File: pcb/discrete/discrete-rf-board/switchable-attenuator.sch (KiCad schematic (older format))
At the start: 11 parts, among them U18 BGS12PL6E6327XTSA1, U19 BGS12PL6E6327XTSA1

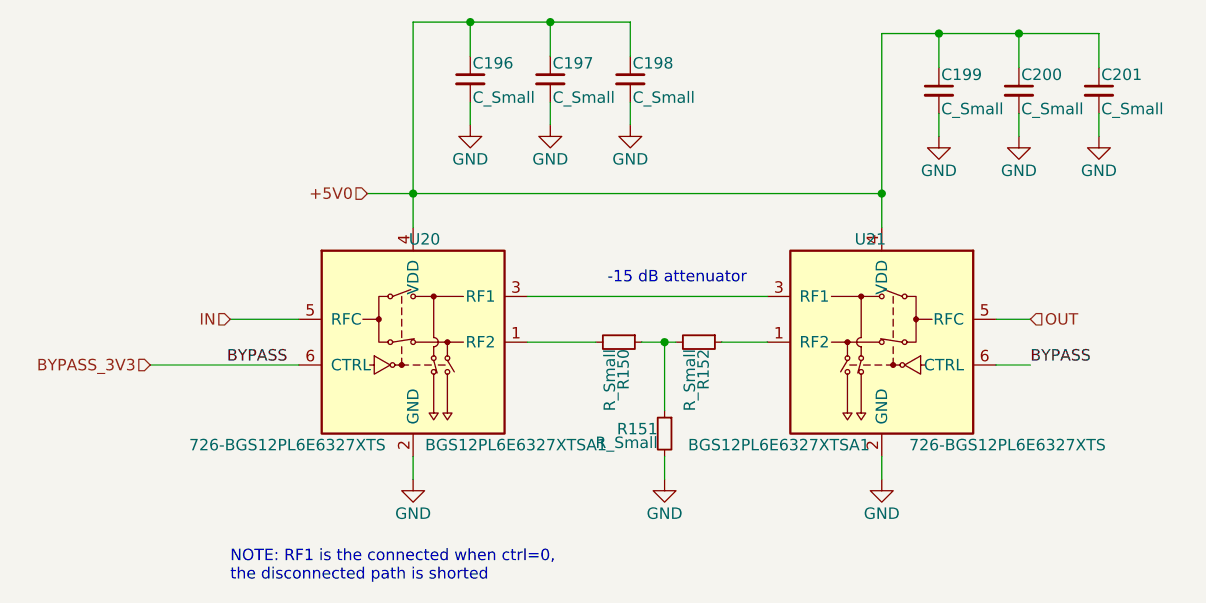
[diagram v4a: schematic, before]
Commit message: All component values set (TODO change transistor gain stages to match values from experimentation
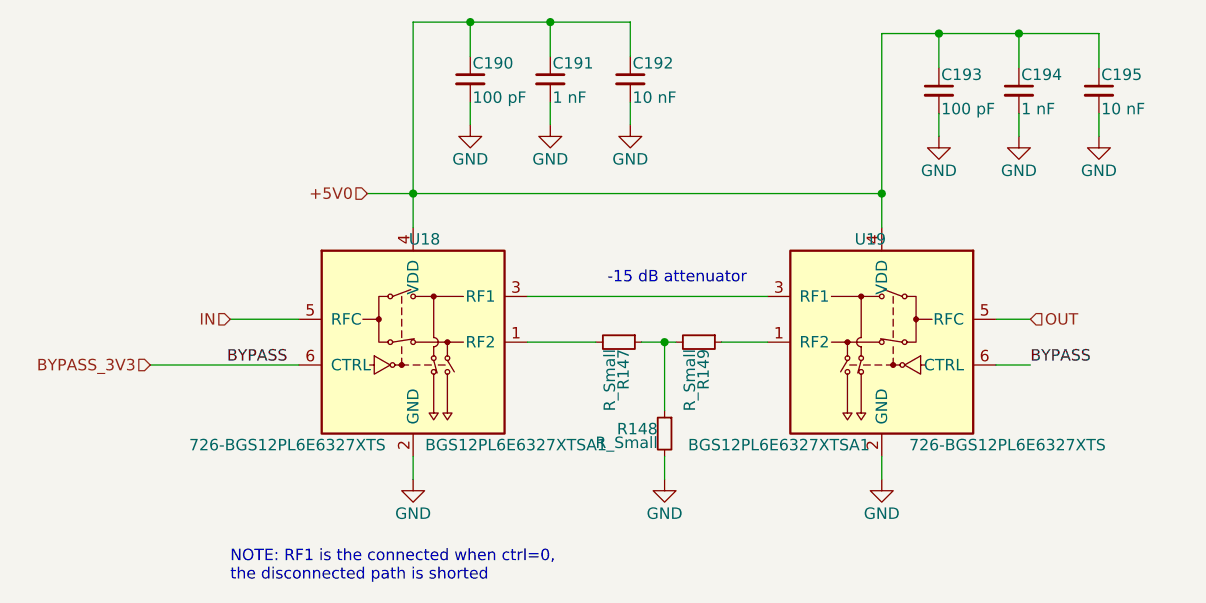
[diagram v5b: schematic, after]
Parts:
- C190, C193: value C_Small -> 100 pF
- C191, C194: value C_Small -> 1 nF
- C192, C195: value C_Small -> 10 nF
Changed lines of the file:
@@
 AR Path="/5CA6B0AA/5CE74EBE/5D4B0AA8/5D4B1FC3" Ref="U18"  Part="1"
 AR Path="/5CA6B0AA/5CE74EBE/5D4C7749/5D4B1FC3" Ref="U20"  Part="1"
-F 0 "U20" H 4000 3750 50  0000 C CNN
+F 0 "U18" H 4000 3750 50  0000 C CNN
 F 1 "BGS12PL6E6327XTSA1" H 4400 2850 50  0000 C CNN
 F 2 "discrete_footprints:Infineon_TSLP-6-4" H 3950 3300 50  0001 C CNN
@@
 AR Path="/5CA6B0AA/5CE74EBE/5D4B0AA8/5D4B1FCA" Ref="R147"  Part="1"
 AR Path="/5CA6B0AA/5CE74EBE/5D4C7749/5D4B1FCA" Ref="R150"  Part="1"
-F 0 "R150" H 4880 3320 50  0000 L CNN
+F 0 "R147" H 4880 3320 50  0000 L CNN
 F 1 "R_Small" H 4880 3260 50  0000 L CNN
 F 2 "" H 4850 3300 50  0001 C CNN
@@
 AR Path="/5CA6B0AA/5CE74EBE/5D4B0AA8/5D4B1FD0" Ref="R149"  Part="1"
 AR Path="/5CA6B0AA/5CE74EBE/5D4C7749/5D4B1FD0" Ref="R152"  Part="1"
-F 0 "R152" H 5230 3320 50  0000 L CNN
+F 0 "R149" H 5230 3320 50  0000 L CNN
 F 1 "R_Small" H 5230 3260 50  0000 L CNN
 F 2 "" H 5200 3300 50  0001 C CNN
@@
 AR Path="/5CA6B0AA/5CE74EBE/5D4B0AA8/5D4B1FD6" Ref="R148"  Part="1"
 AR Path="/5CA6B0AA/5CE74EBE/5D4C7749/5D4B1FD6" Ref="R151"  Part="1"
-F 0 "R151" H 5080 3720 50  0000 L CNN
+F 0 "R148" H 5080 3720 50  0000 L CNN
 F 1 "R_Small" H 5080 3660 50  0000 L CNN
 F 2 "" H 5050 3700 50  0001 C CNN
@@
 AR Path="/5CA6B0AA/5CE74EBE/5D4B0AA8/5D4B1FDD" Ref="#PWR0238"  Part="1"
 AR Path="/5CA6B0AA/5CE74EBE/5D4C7749/5D4B1FDD" Ref="#PWR0247"  Part="1"
-F 0 "#PWR0247" H 3950 3650 50  0001 C CNN
+F 0 "#PWR0238" H 3950 3650 50  0001 C CNN
 F 1 "GND" H 3950 3750 50  0000 C CNN
 F 2 "" H 3950 3900 50  0001 C CNN
@@
 AR Path="/5CA6B0AA/5CE74EBE/5D4B0AA8/5D4B1FE5" Ref="#PWR0242"  Part="1"
 AR Path="/5CA6B0AA/5CE74EBE/5D4C7749/5D4B1FE5" Ref="#PWR0251"  Part="1"
-F 0 "#PWR0251" H 5050 3650 50  0001 C CNN
+F 0 "#PWR0242" H 5050 3650 50  0001 C CNN
 F 1 "GND" H 5050 3750 50  0000 C CNN
 F 2 "" H 5050 3900 50  0001 C CNN
@@
 AR Path="/5CA6B0AA/5CE74EBE/5D4B0AA8/5D4B2001" Ref="#PWR0243"  Part="1"
 AR Path="/5CA6B0AA/5CE74EBE/5D4C7749/5D4B2001" Ref="#PWR0252"  Part="1"
-F 0 "#PWR0252" H 6000 3650 50  0001 C CNN
+F 0 "#PWR0243" H 6000 3650 50  0001 C CNN
 F 1 "GND" H 6000 3750 50  0000 C CNN
 F 2 "" H 6000 3900 50  0001 C CNN
@@
 AR Path="/5CA6B0AA/5CE74EBE/5D4B0AA8/5D4B1FF8" Ref="U19"  Part="1"
 AR Path="/5CA6B0AA/5CE74EBE/5D4C7749/5D4B1FF8" Ref="U21"  Part="1"
-F 0 "U21" H 6050 3750 50  0000 C CNN
+F 0 "U19" H 6050 3750 50  0000 C CNN
 F 1 "BGS12PL6E6327XTSA1" H 6450 2850 50  0000 C CNN
 F 2 "" H 6000 3300 50  0001 C CNN
@@
 AR Path="/5CA6B0AA/5CE74EBE/5D4B0AA8/5D4BC42E" Ref="C190"  Part="1"
 AR Path="/5CA6B0AA/5CE74EBE/5D4C7749/5D4BC42E" Ref="C196"  Part="1"
-F 0 "C196" H 4210 2220 50  0000 L CNN
-F 1 "C_Small" H 4210 2070 50  0000 L CNN
+F 0 "C190" H 4210 2220 50  0000 L CNN
+F 1 "100 pF" H 4210 2070 50  0000 L CNN
 F 2 "" H 4200 2150 50  0001 C CNN
 F 3 "~" H 4200 2150 50  0001 C CNN
@@
 AR Path="/5CA6B0AA/5CE74EBE/5D4B0AA8/5D4BC853" Ref="C191"  Part="1"
 AR Path="/5CA6B0AA/5CE74EBE/5D4C7749/5D4BC853" Ref="C197"  Part="1"
-F 0 "C197" H 4560 2220 50  0000 L CNN
-F 1 "C_Small" H 4560 2070 50  0000 L CNN
+F 0 "C191" H 4560 2220 50  0000 L CNN
+F 1 "1 nF" H 4560 2070 50  0000 L CNN
 F 2 "" H 4550 2150 50  0001 C CNN
 F 3 "~" H 4550 2150 50  0001 C CNN
@@
 AR Path="/5CA6B0AA/5CE74EBE/5D4B0AA8/5D4BCC70" Ref="C192"  Part="1"
 AR Path="/5CA6B0AA/5CE74EBE/5D4C7749/5D4BCC70" Ref="C198"  Part="1"
-F 0 "C198" H 4910 2220 50  0000 L CNN
-F 1 "C_Small" H 4910 2070 50  0000 L CNN
+F 0 "C192" H 4910 2220 50  0000 L CNN
+F 1 "10 nF" H 4910 2070 50  0000 L CNN
 F 2 "" H 4900 2150 50  0001 C CNN
 F 3 "~" H 4900 2150 50  0001 C CNN
@@
 AR Path="/5CA6B0AA/5CE74EBE/5D4B0AA8/5D4BED00" Ref="C193"  Part="1"
 AR Path="/5CA6B0AA/5CE74EBE/5D4C7749/5D4BED00" Ref="C199"  Part="1"
-F 0 "C199" H 6260 2270 50  0000 L CNN
-F 1 "C_Small" H 6260 2120 50  0000 L CNN
+F 0 "C193" H 6260 2270 50  0000 L CNN
+F 1 "100 pF" H 6260 2120 50  0000 L CNN
 F 2 "" H 6250 2200 50  0001 C CNN
 F 3 "~" H 6250 2200 50  0001 C CNN
@@
 AR Path="/5CA6B0AA/5CE74EBE/5D4B0AA8/5D4BED06" Ref="C194"  Part="1"
 AR Path="/5CA6B0AA/5CE74EBE/5D4C7749/5D4BED06" Ref="C200"  Part="1"
-F 0 "C200" H 6610 2270 50  0000 L CNN
-F 1 "C_Small" H 6610 2120 50  0000 L CNN
+F 0 "C194" H 6610 2270 50  0000 L CNN
+F 1 "1 nF" H 6610 2120 50  0000 L CNN
 F 2 "" H 6600 2200 50  0001 C CNN
 F 3 "~" H 6600 2200 50  0001 C CNN
@@
 AR Path="/5CA6B0AA/5CE74EBE/5D4B0AA8/5D4BED0C" Ref="C195"  Part="1"
 AR Path="/5CA6B0AA/5CE74EBE/5D4C7749/5D4BED0C" Ref="C201"  Part="1"
-F 0 "C201" H 6960 2270 50  0000 L CNN
-F 1 "C_Small" H 6960 2120 50  0000 L CNN
+F 0 "C195" H 6960 2270 50  0000 L CNN
+F 1 "10 nF" H 6960 2120 50  0000 L CNN
 F 2 "" H 6950 2200 50  0001 C CNN
 F 3 "~" H 6950 2200 50  0001 C CNN
@@
 AR Path="/5CA6B0AA/5CE74EBE/5D4B0AA8/5D4BF277" Ref="#PWR0246"  Part="1"
 AR Path="/5CA6B0AA/5CE74EBE/5D4C7749/5D4BF277" Ref="#PWR0255"  Part="1"
-F 0 "#PWR0255" H 6950 2150 50  0001 C CNN
+F 0 "#PWR0246" H 6950 2150 50  0001 C CNN
 F 1 "GND" H 6950 2250 50  0000 C CNN
 F 2 "" H 6950 2400 50  0001 C CNN
@@
 AR Path="/5CA6B0AA/5CE74EBE/5D4B0AA8/5D4BF7E8" Ref="#PWR0245"  Part="1"
 AR Path="/5CA6B0AA/5CE74EBE/5D4C7749/5D4BF7E8" Ref="#PWR0254"  Part="1"
-F 0 "#PWR0254" H 6600 2150 50  0001 C CNN
+F 0 "#PWR0245" H 6600 2150 50  0001 C CNN
 F 1 "GND" H 6600 2250 50  0000 C CNN
 F 2 "" H 6600 2400 50  0001 C CNN
@@
 AR Path="/5CA6B0AA/5CE74EBE/5D4B0AA8/5D4BFA67" Ref="#PWR0244"  Part="1"
 AR Path="/5CA6B0AA/5CE74EBE/5D4C7749/5D4BFA67" Ref="#PWR0253"  Part="1"
-F 0 "#PWR0253" H 6250 2150 50  0001 C CNN
+F 0 "#PWR0244" H 6250 2150 50  0001 C CNN
 F 1 "GND" H 6250 2250 50  0000 C CNN
 F 2 "" H 6250 2400 50  0001 C CNN
@@
 AR Path="/5CA6B0AA/5CE74EBE/5D4B0AA8/5D4C425B" Ref="#PWR0241"  Part="1"
 AR Path="/5CA6B0AA/5CE74EBE/5D4C7749/5D4C425B" Ref="#PWR0250"  Part="1"
-F 0 "#PWR0250" H 4900 2100 50  0001 C CNN
+F 0 "#PWR0241" H 4900 2100 50  0001 C CNN
 F 1 "GND" H 4900 2200 50  0000 C CNN
 F 2 "" H 4900 2350 50  0001 C CNN
@@
 AR Path="/5CA6B0AA/5CE74EBE/5D4B0AA8/5D4C4261" Ref="#PWR0240"  Part="1"
 AR Path="/5CA6B0AA/5CE74EBE/5D4C7749/5D4C4261" Ref="#PWR0249"  Part="1"
-F 0 "#PWR0249" H 4550 2100 50  0001 C CNN
+F 0 "#PWR0240" H 4550 2100 50  0001 C CNN
 F 1 "GND" H 4550 2200 50  0000 C CNN
 F 2 "" H 4550 2350 50  0001 C CNN
@@
 AR Path="/5CA6B0AA/5CE74EBE/5D4B0AA8/5D4C4267" Ref="#PWR0239"  Part="1"
 AR Path="/5CA6B0AA/5CE74EBE/5D4C7749/5D4C4267" Ref="#PWR0248"  Part="1"
-F 0 "#PWR0248" H 4200 2100 50  0001 C CNN
+F 0 "#PWR0239" H 4200 2100 50  0001 C CNN
 F 1 "GND" H 4200 2200 50  0000 C CNN
 F 2 "" H 4200 2350 50  0001 C CNN

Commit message: Autofill; lots left to do
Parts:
- U19: footprint (none) -> discrete_footprints:Infineon_TSLP-6-4
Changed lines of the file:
@@
 AR Path="/5CA6B0AA/5CE74EBE/5D4B0AA8/5D4B1FDD" Ref="#PWR0238"  Part="1"
 AR Path="/5CA6B0AA/5CE74EBE/5D4C7749/5D4B1FDD" Ref="#PWR0247"  Part="1"
-F 0 "#PWR0238" H 3950 3650 50  0001 C CNN
+F 0 "#PWR0247" H 3950 3650 50  0001 C CNN
 F 1 "GND" H 3950 3750 50  0000 C CNN
 F 2 "" H 3950 3900 50  0001 C CNN
@@
 AR Path="/5CA6B0AA/5CE74EBE/5D4B0AA8/5D4B1FE5" Ref="#PWR0242"  Part="1"
 AR Path="/5CA6B0AA/5CE74EBE/5D4C7749/5D4B1FE5" Ref="#PWR0251"  Part="1"
-F 0 "#PWR0242" H 5050 3650 50  0001 C CNN
+F 0 "#PWR0251" H 5050 3650 50  0001 C CNN
 F 1 "GND" H 5050 3750 50  0000 C CNN
 F 2 "" H 5050 3900 50  0001 C CNN
@@
 AR Path="/5CA6B0AA/5CE74EBE/5D4B0AA8/5D4B2001" Ref="#PWR0243"  Part="1"
 AR Path="/5CA6B0AA/5CE74EBE/5D4C7749/5D4B2001" Ref="#PWR0252"  Part="1"
-F 0 "#PWR0243" H 6000 3650 50  0001 C CNN
+F 0 "#PWR0252" H 6000 3650 50  0001 C CNN
 F 1 "GND" H 6000 3750 50  0000 C CNN
 F 2 "" H 6000 3900 50  0001 C CNN
@@
 F 0 "U19" H 6050 3750 50  0000 C CNN
 F 1 "BGS12PL6E6327XTSA1" H 6450 2850 50  0000 C CNN
-F 2 "" H 6000 3300 50  0001 C CNN
+F 2 "discrete_footprints:Infineon_TSLP-6-4" H 6000 3300 50  0001 C CNN
 F 3 "" H 6000 3300 50  0001 C CNN
 F 4 "726-BGS12PL6E6327XTS" H 5450 2850 50  0000 C CNN "Mouser"
@@
 AR Path="/5CA6B0AA/5CE74EBE/5D4B0AA8/5D4BF277" Ref="#PWR0246"  Part="1"
 AR Path="/5CA6B0AA/5CE74EBE/5D4C7749/5D4BF277" Ref="#PWR0255"  Part="1"
-F 0 "#PWR0246" H 6950 2150 50  0001 C CNN
+F 0 "#PWR0255" H 6950 2150 50  0001 C CNN
 F 1 "GND" H 6950 2250 50  0000 C CNN
 F 2 "" H 6950 2400 50  0001 C CNN
@@
 AR Path="/5CA6B0AA/5CE74EBE/5D4B0AA8/5D4BF7E8" Ref="#PWR0245"  Part="1"
 AR Path="/5CA6B0AA/5CE74EBE/5D4C7749/5D4BF7E8" Ref="#PWR0254"  Part="1"
-F 0 "#PWR0245" H 6600 2150 50  0001 C CNN
+F 0 "#PWR0254" H 6600 2150 50  0001 C CNN
 F 1 "GND" H 6600 2250 50  0000 C CNN
 F 2 "" H 6600 2400 50  0001 C CNN
@@
 AR Path="/5CA6B0AA/5CE74EBE/5D4B0AA8/5D4BFA67" Ref="#PWR0244"  Part="1"
 AR Path="/5CA6B0AA/5CE74EBE/5D4C7749/5D4BFA67" Ref="#PWR0253"  Part="1"
-F 0 "#PWR0244" H 6250 2150 50  0001 C CNN
+F 0 "#PWR0253" H 6250 2150 50  0001 C CNN
 F 1 "GND" H 6250 2250 50  0000 C CNN
 F 2 "" H 6250 2400 50  0001 C CNN
@@
 AR Path="/5CA6B0AA/5CE74EBE/5D4B0AA8/5D4C425B" Ref="#PWR0241"  Part="1"
 AR Path="/5CA6B0AA/5CE74EBE/5D4C7749/5D4C425B" Ref="#PWR0250"  Part="1"
-F 0 "#PWR0241" H 4900 2100 50  0001 C CNN
+F 0 "#PWR0250" H 4900 2100 50  0001 C CNN
 F 1 "GND" H 4900 2200 50  0000 C CNN
 F 2 "" H 4900 2350 50  0001 C CNN
@@
 AR Path="/5CA6B0AA/5CE74EBE/5D4B0AA8/5D4C4261" Ref="#PWR0240"  Part="1"
 AR Path="/5CA6B0AA/5CE74EBE/5D4C7749/5D4C4261" Ref="#PWR0249"  Part="1"
-F 0 "#PWR0240" H 4550 2100 50  0001 C CNN
+F 0 "#PWR0249" H 4550 2100 50  0001 C CNN
 F 1 "GND" H 4550 2200 50  0000 C CNN
 F 2 "" H 4550 2350 50  0001 C CNN
@@
 AR Path="/5CA6B0AA/5CE74EBE/5D4B0AA8/5D4C4267" Ref="#PWR0239"  Part="1"
 AR Path="/5CA6B0AA/5CE74EBE/5D4C7749/5D4C4267" Ref="#PWR0248"  Part="1"
-F 0 "#PWR0239" H 4200 2100 50  0001 C CNN
+F 0 "#PWR0248" H 4200 2100 50  0001 C CNN
 F 1 "GND" H 4200 2200 50  0000 C CNN
 F 2 "" H 4200 2350 50  0001 C CNN

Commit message: Autofill
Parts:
- C190, C193: footprint (none) -> Capacitor_SMD:C_0402_1005Metric; Mouser (none) -> 791-RF15N101J250CT
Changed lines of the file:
@@
 F 0 "C190" H 4210 2220 50  0000 L CNN
 F 1 "100 pF" H 4210 2070 50  0000 L CNN
-F 2 "" H 4200 2150 50  0001 C CNN
+F 2 "Capacitor_SMD:C_0402_1005Metric" H 4200 2150 50  0001 C CNN
 F 3 "~" H 4200 2150 50  0001 C CNN
+F 4 "791-RF15N101J250CT " H 4200 2150 50  0001 C CNN "Mouser"
 	1    4200 2150
 	1    0    0    -1
@@
 F 0 "C193" H 6260 2270 50  0000 L CNN
 F 1 "100 pF" H 6260 2120 50  0000 L CNN
-F 2 "" H 6250 2200 50  0001 C CNN
+F 2 "Capacitor_SMD:C_0402_1005Metric" H 6250 2200 50  0001 C CNN
 F 3 "~" H 6250 2200 50  0001 C CNN
+F 4 "791-RF15N101J250CT " H 6250 2200 50  0001 C CNN "Mouser"
 	1    6250 2200
 	1    0    0    -1

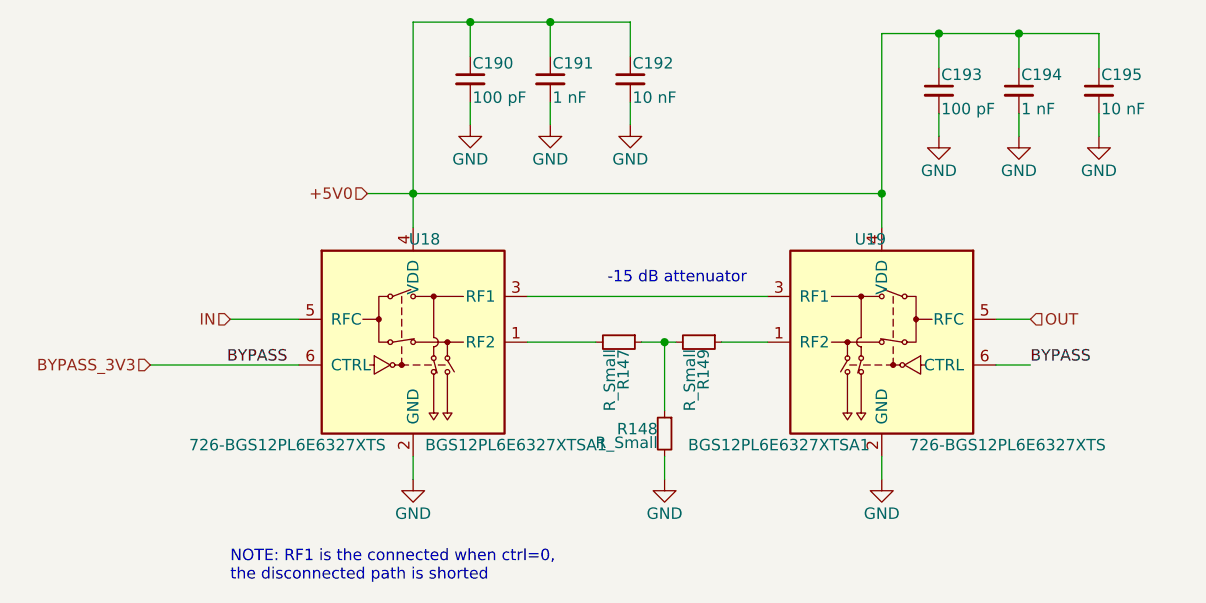
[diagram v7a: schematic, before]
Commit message: Add more footprints, saving before autofill
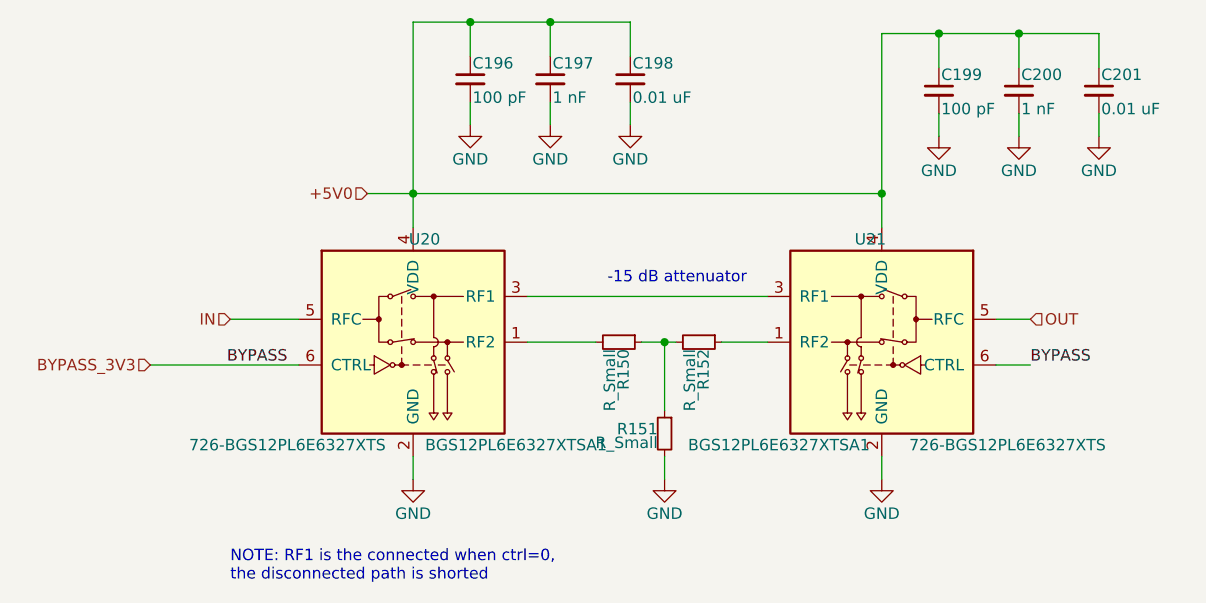
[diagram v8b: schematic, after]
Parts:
- C192, C195: value 10 nF -> 0.01 uF
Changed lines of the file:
@@
 AR Path="/5CA6B0AA/5CE74EBE/5D4B0AA8/5D4B1FC3" Ref="U18"  Part="1"
 AR Path="/5CA6B0AA/5CE74EBE/5D4C7749/5D4B1FC3" Ref="U20"  Part="1"
-F 0 "U18" H 4000 3750 50  0000 C CNN
+F 0 "U20" H 4000 3750 50  0000 C CNN
 F 1 "BGS12PL6E6327XTSA1" H 4400 2850 50  0000 C CNN
 F 2 "discrete_footprints:Infineon_TSLP-6-4" H 3950 3300 50  0001 C CNN
@@
 AR Path="/5CA6B0AA/5CE74EBE/5D4B0AA8/5D4B1FCA" Ref="R147"  Part="1"
 AR Path="/5CA6B0AA/5CE74EBE/5D4C7749/5D4B1FCA" Ref="R150"  Part="1"
-F 0 "R147" H 4880 3320 50  0000 L CNN
+F 0 "R150" H 4880 3320 50  0000 L CNN
 F 1 "R_Small" H 4880 3260 50  0000 L CNN
 F 2 "" H 4850 3300 50  0001 C CNN
@@
 AR Path="/5CA6B0AA/5CE74EBE/5D4B0AA8/5D4B1FD0" Ref="R149"  Part="1"
 AR Path="/5CA6B0AA/5CE74EBE/5D4C7749/5D4B1FD0" Ref="R152"  Part="1"
-F 0 "R149" H 5230 3320 50  0000 L CNN
+F 0 "R152" H 5230 3320 50  0000 L CNN
 F 1 "R_Small" H 5230 3260 50  0000 L CNN
 F 2 "" H 5200 3300 50  0001 C CNN
@@
 AR Path="/5CA6B0AA/5CE74EBE/5D4B0AA8/5D4B1FD6" Ref="R148"  Part="1"
 AR Path="/5CA6B0AA/5CE74EBE/5D4C7749/5D4B1FD6" Ref="R151"  Part="1"
-F 0 "R148" H 5080 3720 50  0000 L CNN
+F 0 "R151" H 5080 3720 50  0000 L CNN
 F 1 "R_Small" H 5080 3660 50  0000 L CNN
 F 2 "" H 5050 3700 50  0001 C CNN
@@
 AR Path="/5CA6B0AA/5CE74EBE/5D4B0AA8/5D4B1FF8" Ref="U19"  Part="1"
 AR Path="/5CA6B0AA/5CE74EBE/5D4C7749/5D4B1FF8" Ref="U21"  Part="1"
-F 0 "U19" H 6050 3750 50  0000 C CNN
+F 0 "U21" H 6050 3750 50  0000 C CNN
 F 1 "BGS12PL6E6327XTSA1" H 6450 2850 50  0000 C CNN
 F 2 "discrete_footprints:Infineon_TSLP-6-4" H 6000 3300 50  0001 C CNN
@@
 AR Path="/5CA6B0AA/5CE74EBE/5D4B0AA8/5D4BC42E" Ref="C190"  Part="1"
 AR Path="/5CA6B0AA/5CE74EBE/5D4C7749/5D4BC42E" Ref="C196"  Part="1"
-F 0 "C190" H 4210 2220 50  0000 L CNN
+F 0 "C196" H 4210 2220 50  0000 L CNN
 F 1 "100 pF" H 4210 2070 50  0000 L CNN
 F 2 "Capacitor_SMD:C_0402_1005Metric" H 4200 2150 50  0001 C CNN
@@
 AR Path="/5CA6B0AA/5CE74EBE/5D4B0AA8/5D4BC853" Ref="C191"  Part="1"
 AR Path="/5CA6B0AA/5CE74EBE/5D4C7749/5D4BC853" Ref="C197"  Part="1"
-F 0 "C191" H 4560 2220 50  0000 L CNN
+F 0 "C197" H 4560 2220 50  0000 L CNN
 F 1 "1 nF" H 4560 2070 50  0000 L CNN
 F 2 "" H 4550 2150 50  0001 C CNN
@@
 AR Path="/5CA6B0AA/5CE74EBE/5D4B0AA8/5D4BCC70" Ref="C192"  Part="1"
 AR Path="/5CA6B0AA/5CE74EBE/5D4C7749/5D4BCC70" Ref="C198"  Part="1"
-F 0 "C192" H 4910 2220 50  0000 L CNN
-F 1 "10 nF" H 4910 2070 50  0000 L CNN
+F 0 "C198" H 4910 2220 50  0000 L CNN
+F 1 "0.01 uF" H 4910 2070 50  0000 L CNN
 F 2 "" H 4900 2150 50  0001 C CNN
 F 3 "~" H 4900 2150 50  0001 C CNN
@@
 AR Path="/5CA6B0AA/5CE74EBE/5D4B0AA8/5D4BED00" Ref="C193"  Part="1"
 AR Path="/5CA6B0AA/5CE74EBE/5D4C7749/5D4BED00" Ref="C199"  Part="1"
-F 0 "C193" H 6260 2270 50  0000 L CNN
+F 0 "C199" H 6260 2270 50  0000 L CNN
 F 1 "100 pF" H 6260 2120 50  0000 L CNN
 F 2 "Capacitor_SMD:C_0402_1005Metric" H 6250 2200 50  0001 C CNN
@@
 AR Path="/5CA6B0AA/5CE74EBE/5D4B0AA8/5D4BED06" Ref="C194"  Part="1"
 AR Path="/5CA6B0AA/5CE74EBE/5D4C7749/5D4BED06" Ref="C200"  Part="1"
-F 0 "C194" H 6610 2270 50  0000 L CNN
+F 0 "C200" H 6610 2270 50  0000 L CNN
 F 1 "1 nF" H 6610 2120 50  0000 L CNN
 F 2 "" H 6600 2200 50  0001 C CNN
@@
 AR Path="/5CA6B0AA/5CE74EBE/5D4B0AA8/5D4BED0C" Ref="C195"  Part="1"
 AR Path="/5CA6B0AA/5CE74EBE/5D4C7749/5D4BED0C" Ref="C201"  Part="1"
-F 0 "C195" H 6960 2270 50  0000 L CNN
-F 1 "10 nF" H 6960 2120 50  0000 L CNN
+F 0 "C201" H 6960 2270 50  0000 L CNN
+F 1 "0.01 uF" H 6960 2120 50  0000 L CNN
 F 2 "" H 6950 2200 50  0001 C CNN
 F 3 "~" H 6950 2200 50  0001 C CNN
